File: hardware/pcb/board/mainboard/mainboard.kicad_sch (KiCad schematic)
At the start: 130 parts, among them J1 Conn_Coaxial, J10 USB_C_Receptacle, J11 2908-05WB-MG, J2 BATTERY_Insta_360_Ace_Pro, J3 Conn_02x35_Odd_Even_MountingP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, J4 Conn_02x40_Odd_Even_MountingP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, J5 Conn_02x40_Odd_Even_MountingP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, J6 USB_C_Receptacle, J7 Conn_01x30, J8 Conn_01x30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

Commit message: parts placement
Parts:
- removed TP1: TestPoint, TestPoint:TestPoint_Pad_D1.5mm, symbol Connector:TestPoint
- added C38: 100 nF, Capacitor_SMD:C_0603_1608Metric, symbol Device:C_Small
- added D8: LED, LED_SMD:LED_0603_1608Metric, symbol Device:LED
- added R32: 100k, Resistor_SMD:R_0603_1608Metric, symbol Device:R_Small
- J1: footprint Connector_Coaxial:SMA_Molex_73251-2200_Horizontal -> Connector_Coaxial:MMCX_Molex_73415-0961_Horizontal_1.6mm-PCB
- J10, J6: footprint Connector_USB:USB_C_Receptacle_Amphenol_12401548E4-2A -> Connector_USB:USB_C_CONN_1054550101_MOL
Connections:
- net GND: now also C38.2, D8.1 (K)
- net USB_PD: now also R32.1
- net VBUS: now also C38.1
- net V_BCKP: now also C6.1, R1.1
- net at BT1.1 (+), JP1.1 (A): no longer C6.1, R1.1
- new net: D8.2 (A), R32.2
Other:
- note added: "# TODO - check coax conn type for antennas - TP everything! - 0 ohm connections - add way for cam0 cam1 slave master operation? - TXS0102 logic lvl shifter - WATCH FOR INVERSE PINS WHEN SWITCHING SIDE FOR CAM 0 / 1 - transfer SOM based MIPI to CAM connection via FPC"
- note removed: "# TODO - TP everything! - 0 ohm connections - add way for cam0 cam1 slave master operation? - TXS0102 logic lvl shifter - WATCH FOR INVERSE PINS WHEN SWITCHING SIDE FOR CAM 0 / 1 - transfer SOM based MIPI to CAM connection via FPC"
- moved on the sheet: BT1, JP1

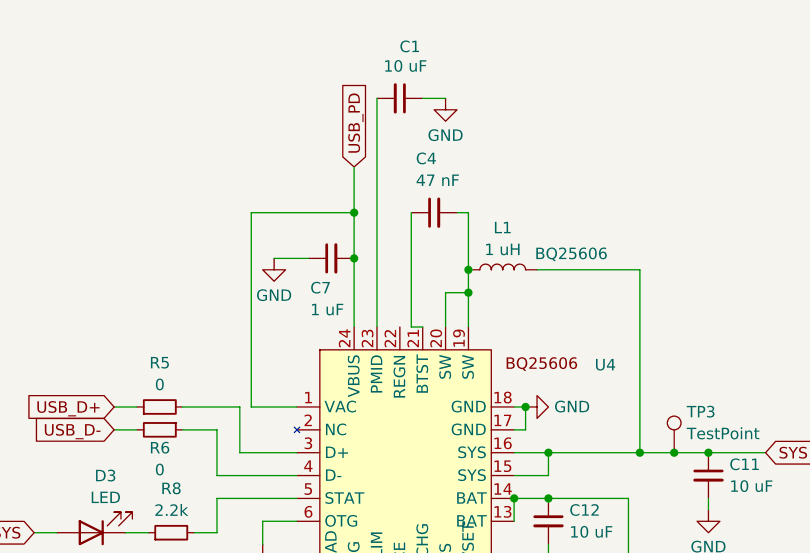
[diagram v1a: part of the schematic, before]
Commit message: preliminary placement of all parts
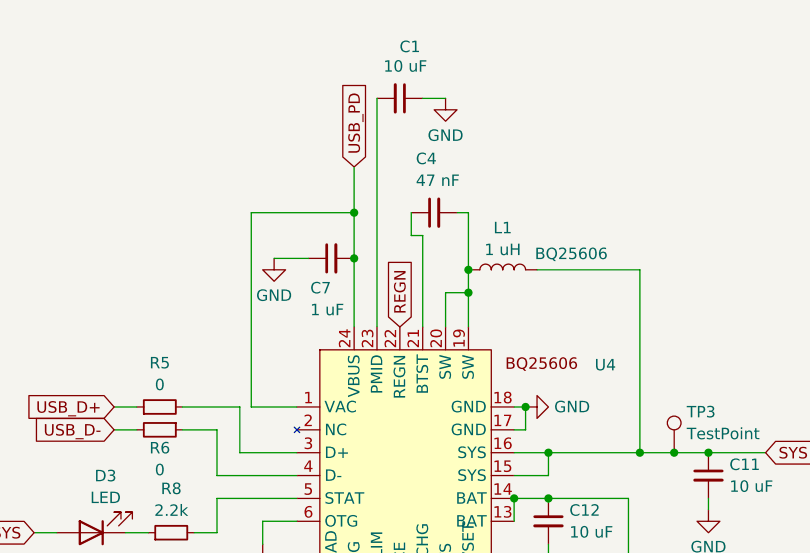
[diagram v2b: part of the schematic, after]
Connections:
- net REGN: now also U4.22 (REGN)
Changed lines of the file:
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@@
 	(wire
 		(pts
+			(xy 76.2 50.8) (xy 76.2 40.64)
+		)
+		(stroke
+			(width 0)
+			(type default)
+		)
+	)
+	(wire
+		(pts
 			(xy 351.79 401.32) (xy 354.33 401.32)
 		)
@@
 	(wire
 		(pts
-			(xy 74.93 50.8) (xy 74.93 38.1)
-		)
-		(stroke
-			(width 0)
-			(type default)
-		)
-	)
-	(wire
-		(pts
 			(xy 101.6 295.91) (xy 101.6 299.72)
 		)
@@
 	(wire
 		(pts
-			(xy 76.2 50.8) (xy 74.93 50.8)
-		)
-		(stroke
-			(width 0)
-			(type default)
-		)
-	)
-	(wire
-		(pts
 			(xy 53.34 69.85) (xy 62.23 69.85)
 		)
@@
 	(wire
 		(pts
+			(xy 76.2 40.64) (xy 74.93 40.64)
+		)
+		(stroke
+			(width 0)
+			(type default)
+		)
+	)
+	(wire
+		(pts
 			(xy 86.36 62.23) (xy 87.63 62.23)
 		)
@@
 	(wire
 		(pts
+			(xy 74.93 40.64) (xy 74.93 38.1)
+		)
+		(stroke
+			(width 0)
+			(type default)
+		)
+	)
+	(wire
+		(pts
 			(xy 154.94 360.68) (xy 177.8 360.68)
 		)
@@
 			(effects
 				(font
+					(size 1.27 1.27)
+				)
+				(justify left)
+				(hide yes)
+			)
+		)
+	)
+	(global_label "REGN"
+		(shape input)
+		(at 73.66 50.8 90)
+		(fields_autoplaced yes)
+		(effects
+			(font
+				(size 1.27 1.27)
+			)
+			(justify left)
+		)
+		(property "Intersheetrefs" "${INTERSHEET_REFS}"
+			(at 73.66 42.7953 90)
+			(effects
+				(font

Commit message: replace battery with dual 18350
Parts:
- removed J2: BATTERY_Insta_360_Ace_Pro, Connector_PinHeader_2.00mm:PinHeader_1x04_P2.00mm_Vertical, symbol Connector:Conn_01x04_Pin
- added BT2: dual_18350_battery, unsurv_offline_pcb_footprints:keystone_dual_18350, symbol unsurv_offline_pcb_symbols:dual_18350_battery
- J1: footprint Connector_Coaxial:MMCX_Molex_73415-0961_Horizontal_1.6mm-PCB -> unsurv_offline_pcb_footprints:MOLEX_SMA_0732511143
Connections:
- net B+: now also BT2.1 (+)
- net B-: now also BT2.2 (-)
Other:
- note added: "# TODO active antenna connection + choose new SMA connector with no board cutout"
- note added: "# TODO edit charge current for dual 18350"
- note added: "# TODO edit end charge to 4.2V"
- note removed: "palceholder connector used here"
- moved on the sheet: BT1, C6, D1, J1, JP1, R1, R10, R2, R3, TP6, U3

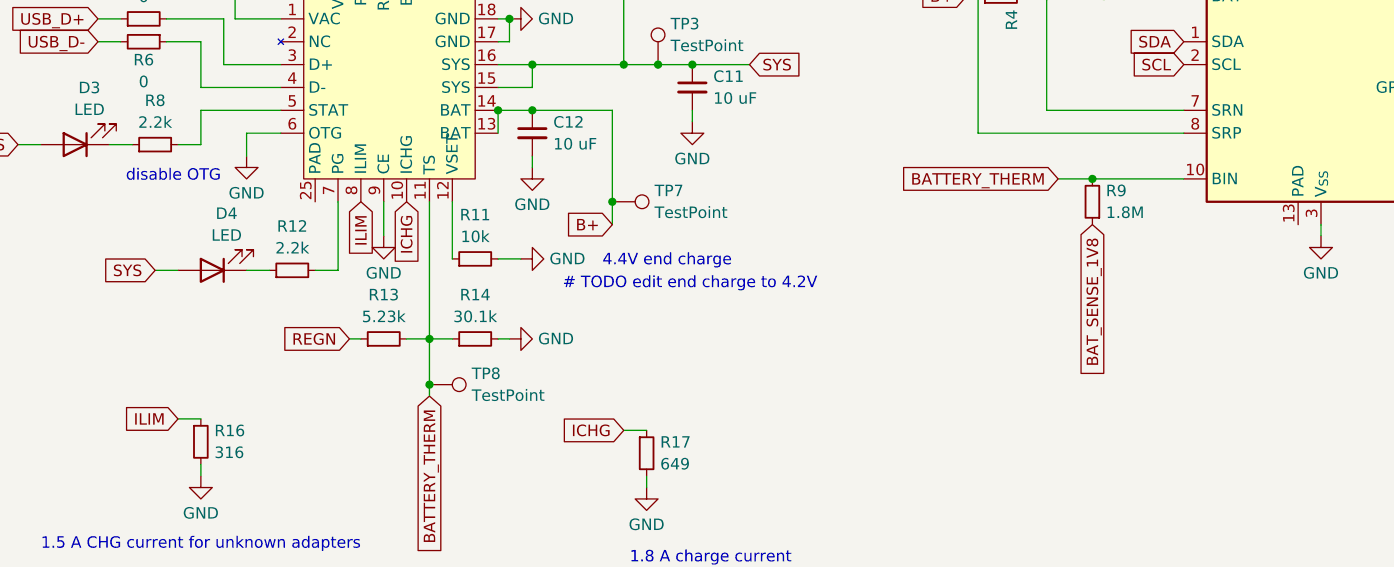
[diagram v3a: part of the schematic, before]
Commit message: organize PCB around new battery holder
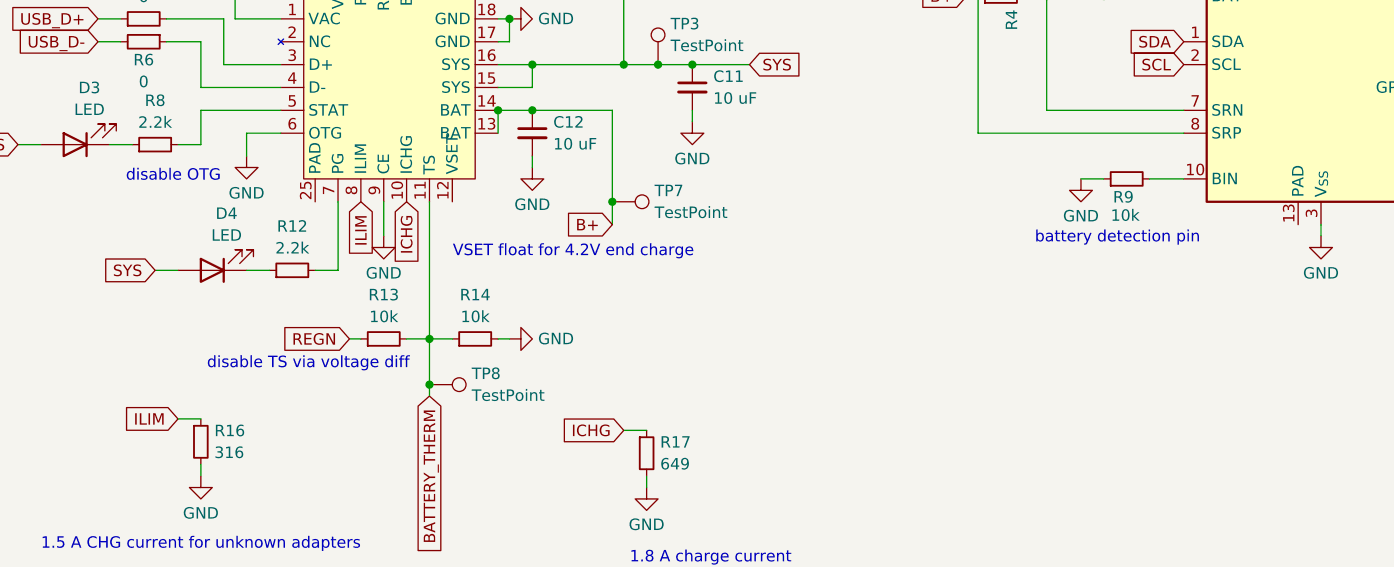
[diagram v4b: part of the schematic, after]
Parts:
- removed R11: 10k, Resistor_SMD:R_0603_1608Metric, symbol Device:R_Small
- R13: value 5.23k -> 10k
- R14: value 30.1k -> 10k
- R9: value 1.8M -> 10k
- U10: footprint Package_SO:SSOP-28_5.3x10.2mm_P0.65mm -> Package_DFN_QFN:QFN-32-1EP_5x5mm_P0.5mm_EP3.65x3.65mm
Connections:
- net BATTERY_THERM: no longer R9.2, U5.10 (BIN)
- net BAT_SENSE_1V8: no longer R9.1
- net GND: now also R9.1
- new net: R9.2, U5.10 (BIN)
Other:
- note added: "VSET float for 4.2V end charge"
- note added: "battery detection pin"
- note added: "disable TS via voltage diff"
- note removed: "# TODO edit end charge to 4.2V"
- note removed: "4.4V end charge"

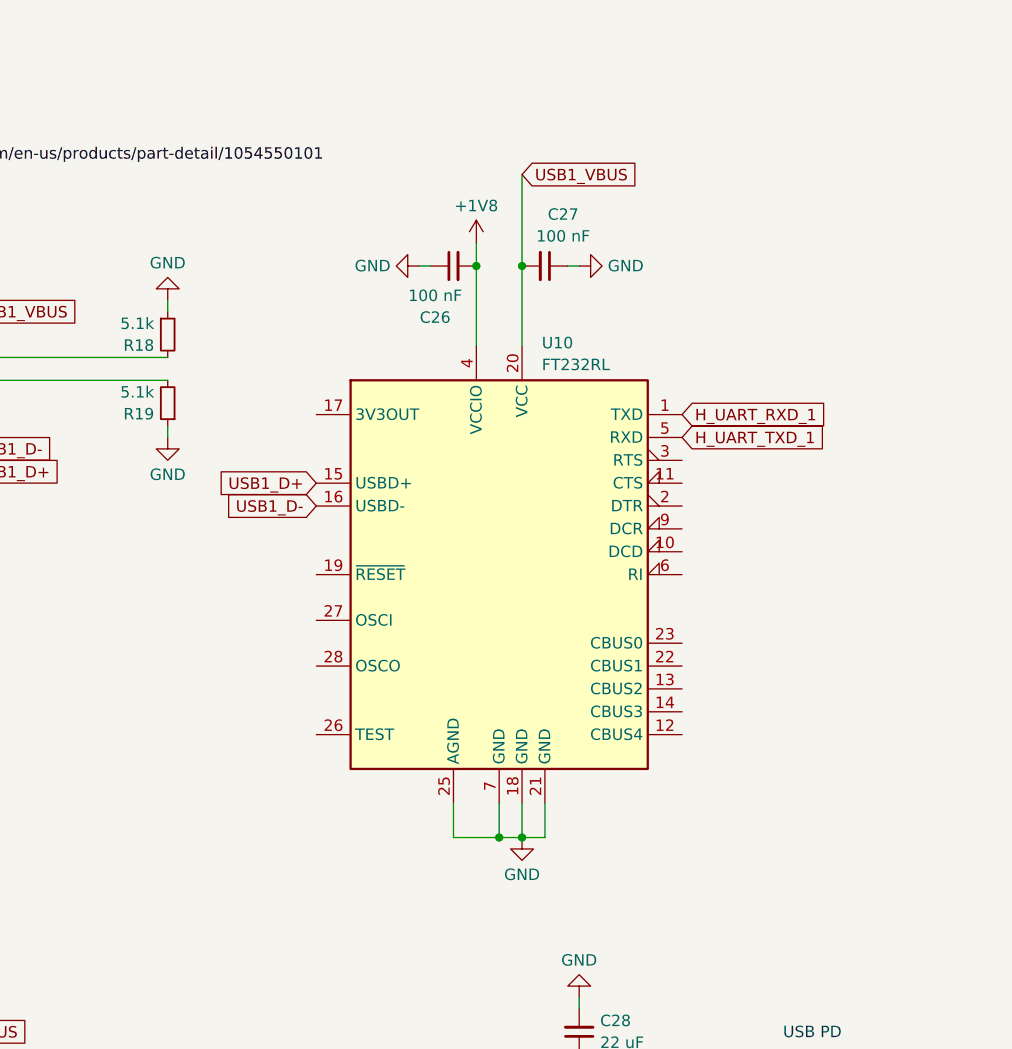
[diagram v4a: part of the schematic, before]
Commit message: replace FTDI with DFN12 package
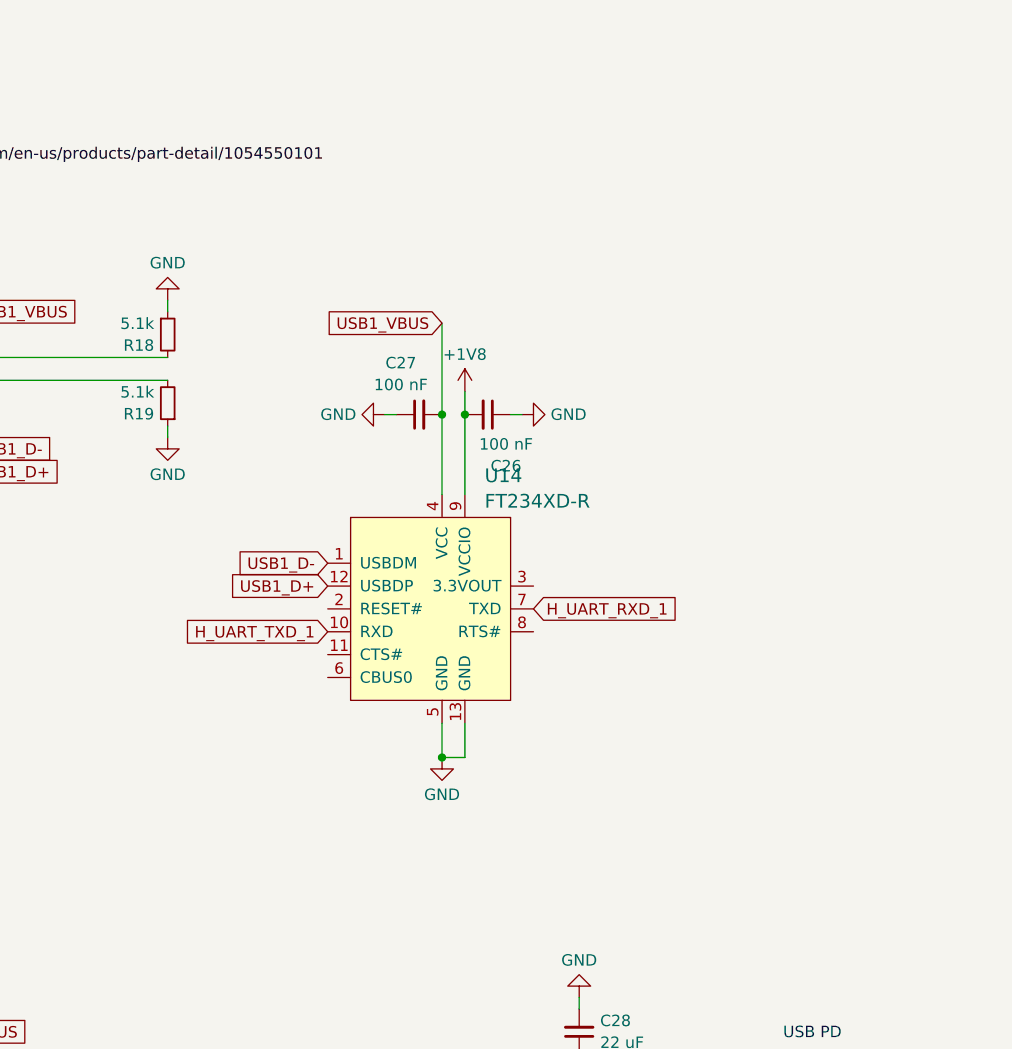
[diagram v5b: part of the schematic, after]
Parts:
- removed U10: FT232RL, Package_DFN_QFN:QFN-32-1EP_5x5mm_P0.5mm_EP3.65x3.65mm, symbol Interface_USB:FT232RL
- added U14: FT234XD-R, digikey-footprints:DFN-12-1EP_3x3mm, symbol dk_Interface-Controllers:FT234XD-R
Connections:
- net +1V8: now also U14.9 (VCCIO)
- net GND: now also U14.13 (GND), U14.5 (GND)
- net H_UART_RXD_1: now also U14.7 (TXD)
- net H_UART_TXD_1: now also U14.10 (RXD)
- net USB1_D+: now also U14.12 (USBDP)
- net USB1_D-: now also U14.1 (USBDM)
- net USB1_VBUS: now also U14.4 (VCC)
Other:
- moved on the sheet: C26, C27

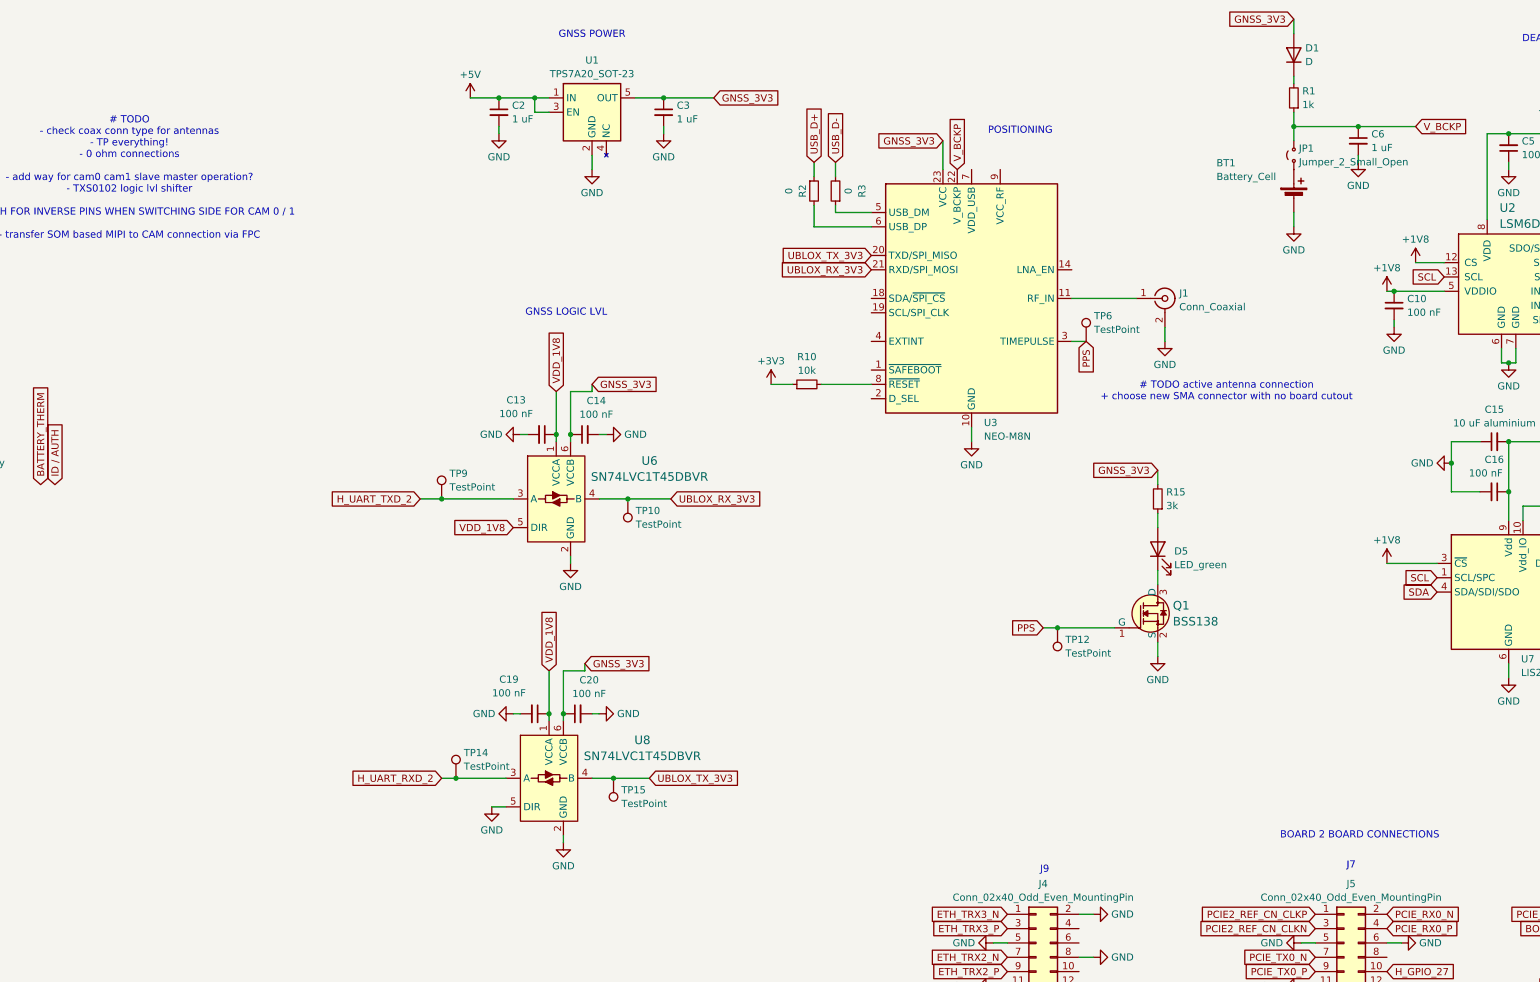
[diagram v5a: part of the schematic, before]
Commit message: update active antenna design
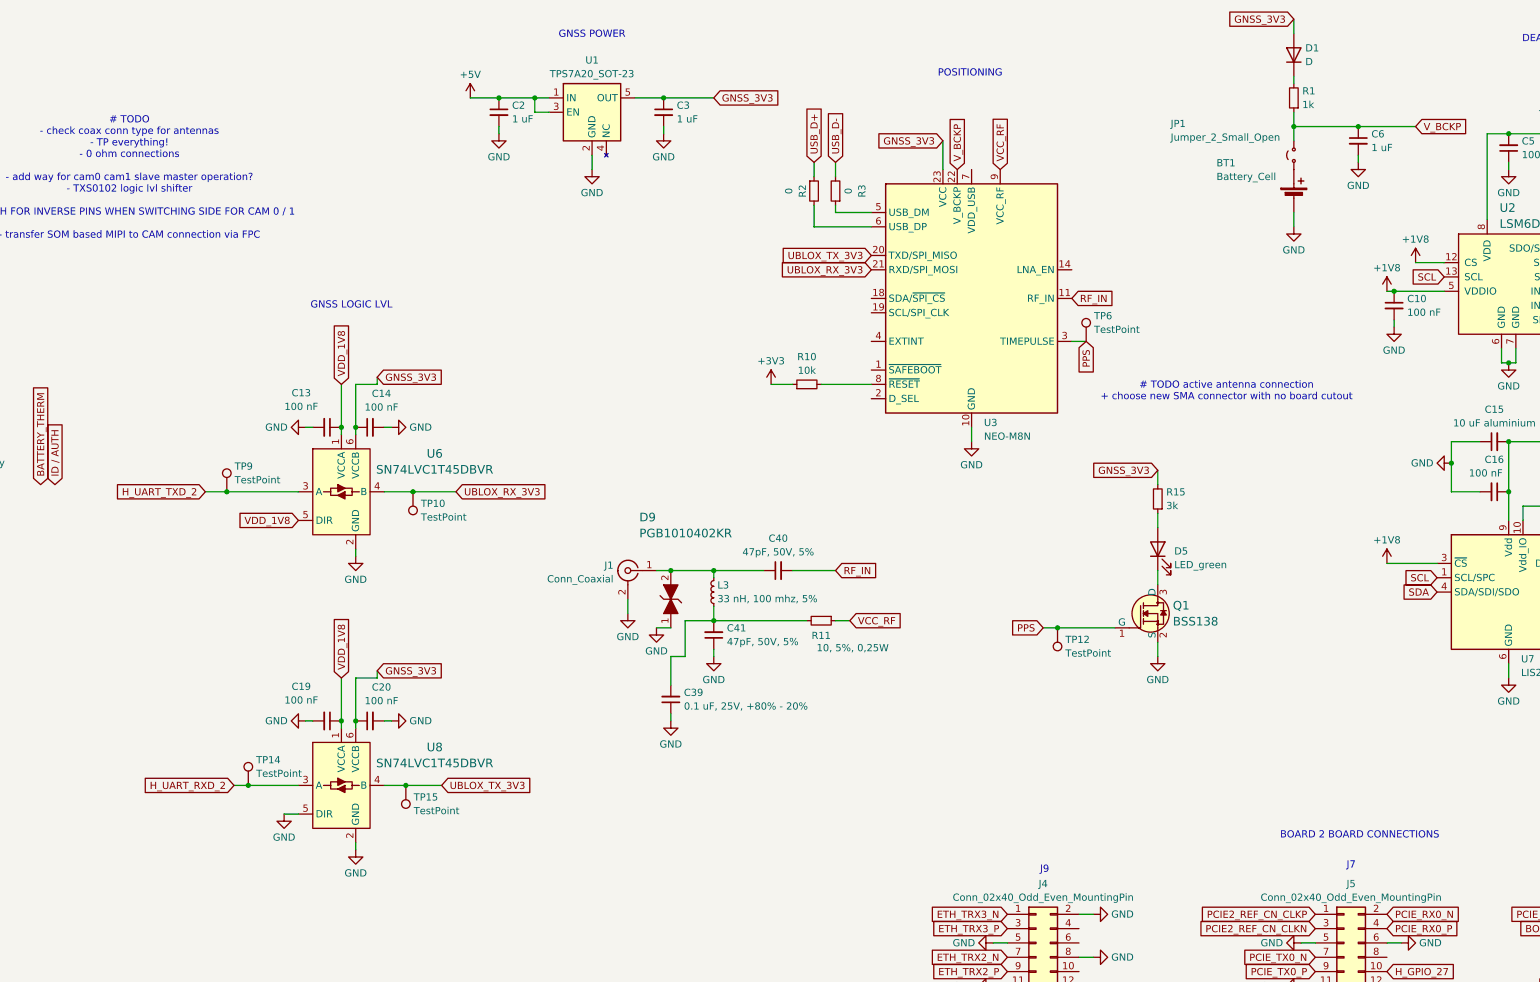
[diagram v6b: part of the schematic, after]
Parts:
- added C39: 0.1 uF, 25V, +80% - 20%, Capacitor_SMD:C_0603_1608Metric, symbol Device:C_Small
- added C40, C41: 47pF, 50V, 5%, Capacitor_SMD:C_0603_1608Metric, symbol Device:C_Small
- added D9: PGB1010402KR, Diode_SMD:D_0402_1005Metric, symbol dk_TVS-Diodes:PGB1010603MR
- added L3: 33 nH, 100 mhz, 5%, Inductor_SMD:L_0402_1005Metric, symbol Device:L_Small
- added R11: 10, 5%, 0,25W, Resistor_SMD:R_0603_1608Metric, symbol Device:R_Small
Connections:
- net GND: now also C39.1, C41.1, D9.1
- net at J1.1 (In): now also C40.1, D9.2, L3.2; no longer U3.11 (RF_IN)
- net VCC_RF: now reaches U3.9 (VCC_RF)
- net VCC_RF: now also R11.1
- new net: C39.2, C41.2, L3.1, R11.2
- new net RF_IN: C40.2, U3.11 (RF_IN)
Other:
- moved on the sheet: C13, C14, C19, C20, J1, TP10, TP14, TP15, TP9, U6, U8

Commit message: update SMA receptable
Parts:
- J1: footprint unsurv_offline_pcb_footprints:MOLEX_SMA_0732511143 -> unsurv_offline_pcb_footprints:RF_SMA_Receptical_Vertical_CONSMA002-SMD-G
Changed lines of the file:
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@@
 			)
 		)
-		(property "Footprint" "unsurv_offline_pcb_footprints:MOLEX_SMA_0732511143"
+		(property "Footprint" "unsurv_offline_pcb_footprints:RF_SMA_Receptical_Vertical_CONSMA002-SMD-G"
 			(at 367.03 113.03 0)
 			(effects
